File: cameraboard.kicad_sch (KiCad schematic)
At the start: 13 parts, among them J1 02x10 1.27mm, J2 Micro_SD_Card, J3 Conn 01x10 1.27mm, Q1 Nikla_Vision, Q2 SSM3J133TU,LF

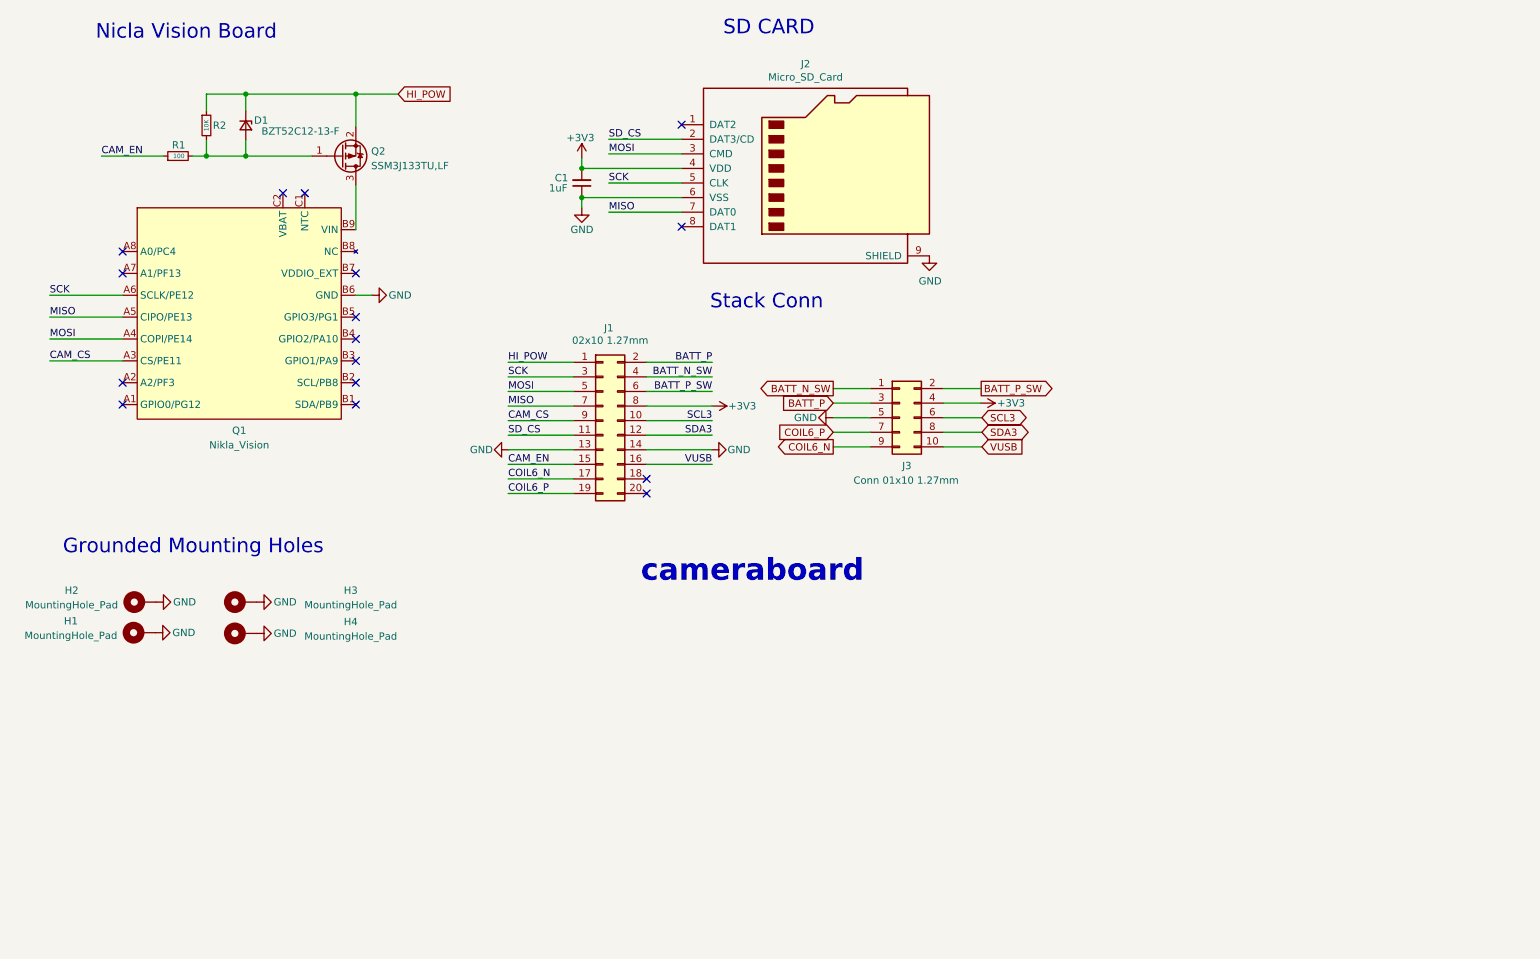
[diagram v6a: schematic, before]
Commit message: Moved Camera slightly, added bus protection
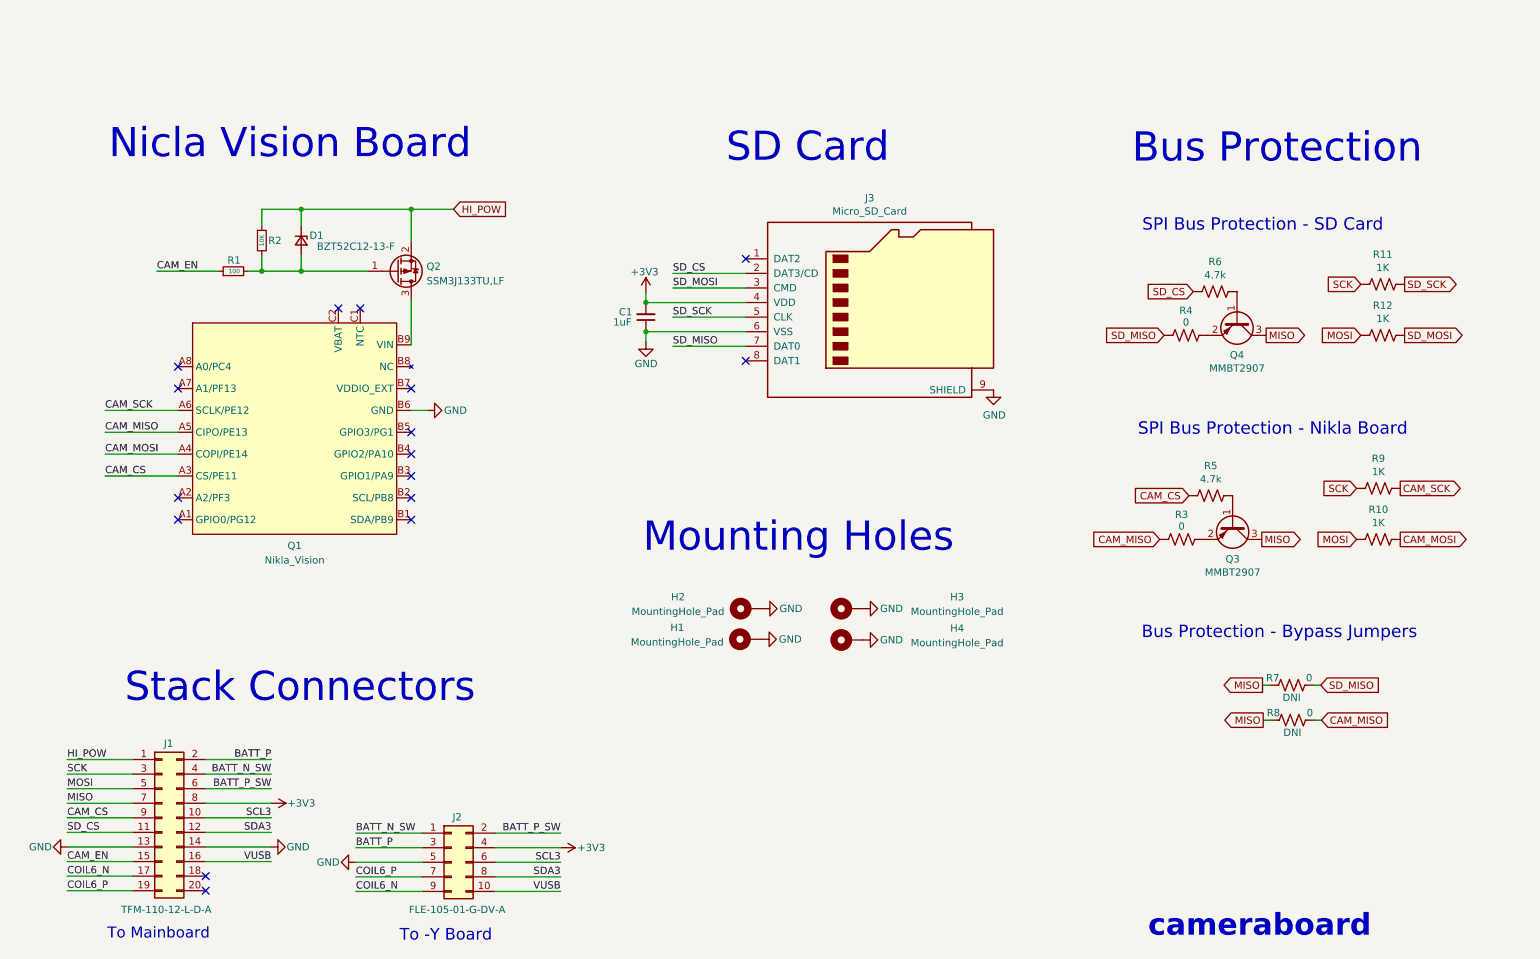
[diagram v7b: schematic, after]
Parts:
- added Q3, Q4: MMBT2907, Package_TO_SOT_SMD:SOT-23, symbol mainboard:MMBT2907
- added R10, R11, R12, R9: 1K, Resistor_SMD:R_0603_1608Metric, symbol Device:R_US
- added R3, R4, R7, R8: 0, Resistor_SMD:R_0603_1608Metric, symbol Device:R_US
- added R5, R6: 4.7k, Resistor_SMD:R_0603_1608Metric, symbol Device:R_US
- J1: value 02x10 1.27mm -> TFM-110-12-L-D-A
- J2: renamed from J3; value Conn 01x10 1.27mm -> FLE-105-01-G-DV-A
- renumbered J2 to J3
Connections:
- net CAM_CS: now also R5.2
- net MISO: now also Q3.3 (C), Q4.3 (C), R7.2, R8.2; no longer J3.7 (DAT0), Q1.A5 (CIPO/PE13)
- net MOSI: now also R10.2, R12.2; no longer J3.3 (CMD), Q1.A4 (COPI/PE14)
- net SCK: now also R11.2, R9.2; no longer J3.5 (CLK), Q1.A6 (SCLK/PE12)
- net SD_CS: now also R6.2
- new net: Q4.1 (B), R6.1
- new net: Q3.2 (E), R3.1
- new net: Q4.2 (E), R4.1
- new net: Q3.1 (B), R5.1
- new net CAM_MISO: Q1.A5 (CIPO/PE13), R3.2, R8.1
- new net CAM_MOSI: Q1.A4 (COPI/PE14), R10.1
- new net CAM_SCK: Q1.A6 (SCLK/PE12), R9.1
- new net SD_MISO: J3.7 (DAT0), R4.2, R7.1
- new net SD_MOSI: J3.3 (CMD), R12.1
- new net SD_SCK: J3.5 (CLK), R11.1
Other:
- note added: "Bus Protection"
- note added: "Bus Protection - Bypass Jumpers"
- note added: "Mounting Holes"
- note added: "SD Card"
- note added: "SPI Bus Protection - Nikla Board"
- note added: "SPI Bus Protection - SD Card"
- note added: "Stack Connectors"
- note added: "To -Y Board"
- note added: "To Mainboard"
- note removed: "Grounded Mounting Holes"
- note removed: "SD CARD"
- note removed: "Stack Conn"
- moved on the sheet: C1, D1, H1, H2, H3, H4, J1, J2, J3, Q1, Q2, R1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

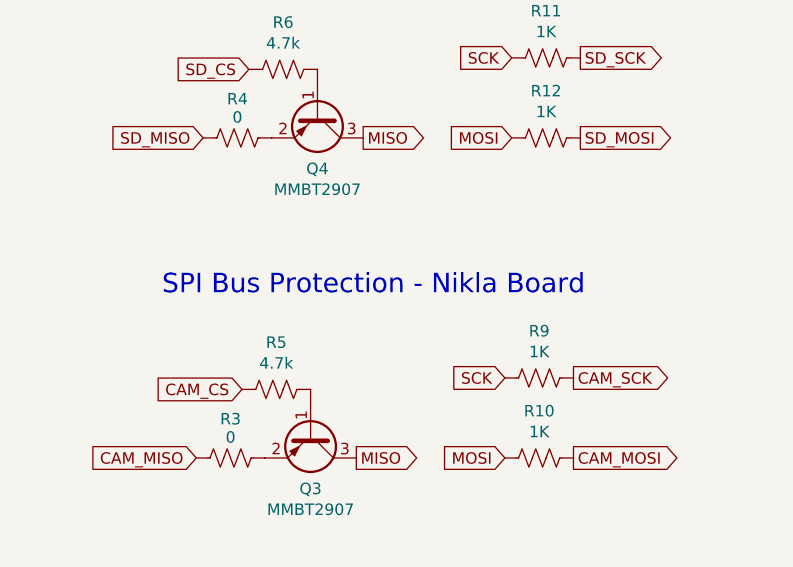
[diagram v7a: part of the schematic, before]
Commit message: nikla -> nicla
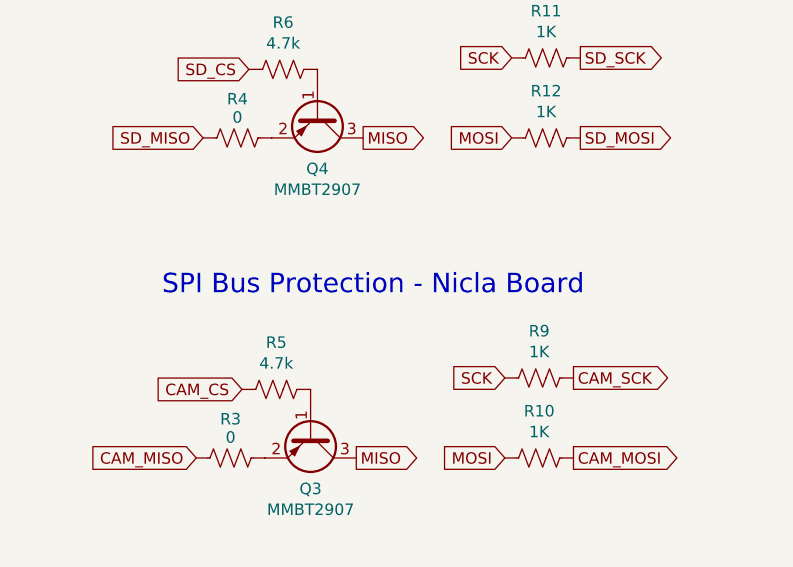
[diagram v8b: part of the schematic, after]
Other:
- note added: "SPI Bus Protection - Nicla Board"
- note removed: "SPI Bus Protection - Nikla Board"
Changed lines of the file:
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@@
     (effects (font (size 3.81 3.81) (thickness 0.762) bold) (justify left bottom))
   )
-  (text "SPI Bus Protection - Nikla Board" (at 211.836 89.027 0)
+  (text "SPI Bus Protection - Nicla Board" (at 211.836 89.027 0)
     (effects (font (size 2.159 2.159)) (justify left bottom))
   )
